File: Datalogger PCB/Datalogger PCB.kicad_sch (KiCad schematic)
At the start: 50 parts, among them J1 Conn_01x02_Pin, M1 Motor_Servo, M2 Motor_Servo, M3 Motor_Servo, M4 Motor_Servo, U1 Teensy4.1, U2 BNO055, U3 LPS25HB, U4 AMS1117-5.0, U5 NRF24L01_Breakout, U6 VN5E160STR-E, U7 VN5E160STR-E, U8 VN5E160STR-E, U9 VN5E160STR-E

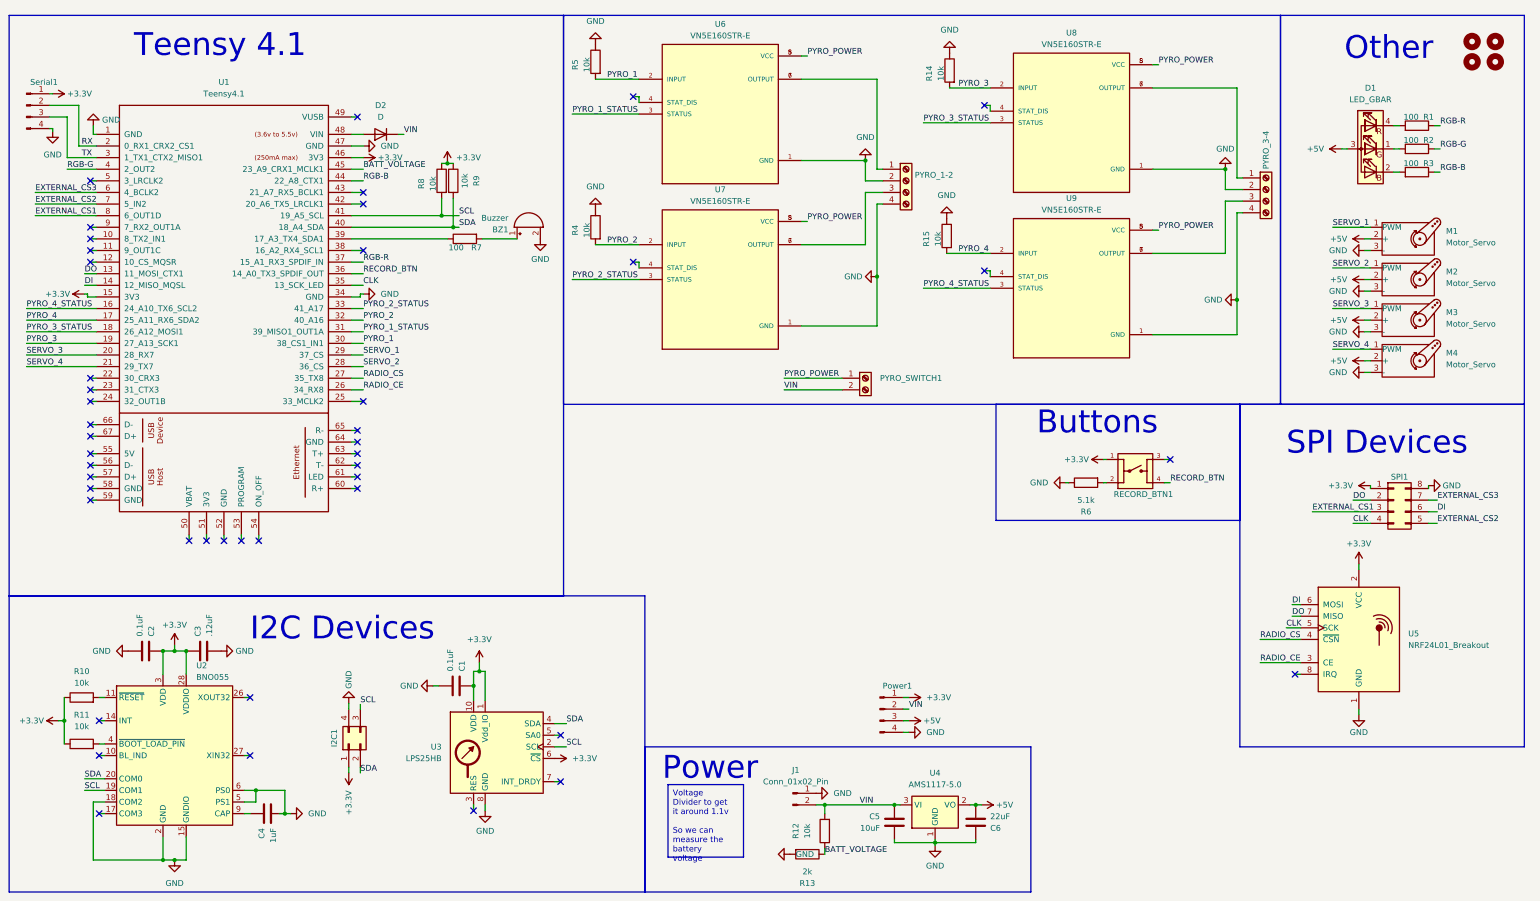
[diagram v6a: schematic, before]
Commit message: Modified the 5v power rail a little
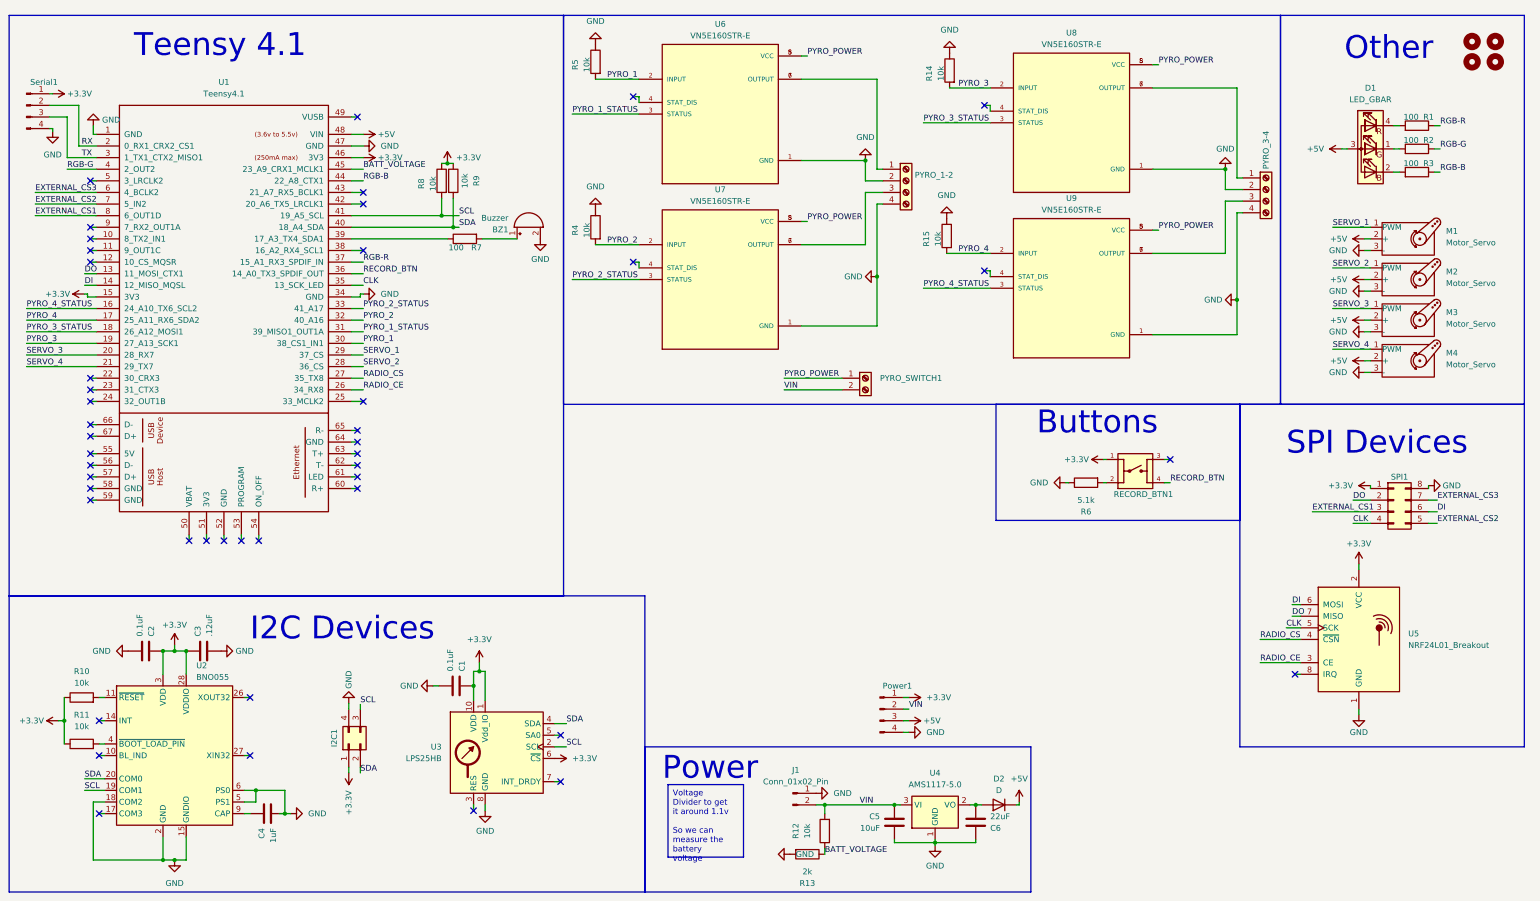
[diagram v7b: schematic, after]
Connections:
- net +5V: now also D2.1 (K), U1.48 (VIN); no longer C6.2, U4.2 (VO)
- net VIN: no longer D2.1 (K)
- net at D2.2 (A): now also C6.2, U4.2 (VO); no longer U1.48 (VIN)
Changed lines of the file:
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@@
   (junction (at 278.13 45.72) (diameter 0) (color 0 0 0 0)
   )
+  (junction (at 223.52 184.785) (diameter 0) (color 0 0 0 0)
+  )
   (junction (at 214.63 193.04) (diameter 0) (color 0 0 0 0)
   )
@@
   (junction (at 66.04 181.61) (diameter 0) (color 0 0 0 0)
   )
-  (junction (at 223.52 184.785) (diameter 0) (color 0 0 0 0)
-  )
   (junction (at 190.5 184.785) (diameter 0) (color 0 0 0 0)
   )
@@
     (stroke (width 0) (type default))
   )
+  (wire (pts (xy 233.045 184.15) (xy 233.045 184.785))
+    (stroke (width 0) (type default))
+  )
   (wire (pts (xy 301.625 76.2) (xy 309.88 76.2))
     (stroke (width 0) (type default))
@@
     (stroke (width 0) (type default))
   )
-  (wire (pts (xy 89.535 38.1) (xy 86.995 38.1))
+  (wire (pts (xy 233.045 184.785) (xy 232.41 184.785))
     (stroke (width 0) (type default))
   )
@@
     (stroke (width 0) (type default))
   )
+  (wire (pts (xy 224.79 184.785) (xy 223.52 184.785))
+    (stroke (width 0) (type default))
+  )
   (wire (pts (xy 307.34 165.1) (xy 307.34 163.83))
     (stroke (width 0) (type default))
@@
     (stroke (width 0) (type default))
   )
-  (wire (pts (xy 224.79 184.785) (xy 223.52 184.785))
-    (stroke (width 0) (type default))
-  )
   (wire (pts (xy 88.9 176.53) (xy 88.9 177.8))
     (stroke (width 0) (type default))
@@
     (stroke (width 0) (type default))
   )
+  (wire (pts (xy 89.535 38.1) (xy 86.995 38.1))
+    (stroke (width 0) (type default))
+  )
   (wire (pts (xy 21.59 36.83) (xy 20.955 36.83))
     (stroke (width 0) (type default))
@@
     (stroke (width 0) (type default))
   )
-  (wire (pts (xy 98.425 38.1) (xy 97.155 38.1))
-    (stroke (width 0) (type default))
-  )
   (wire (pts (xy 148.59 66.04) (xy 149.86 66.04))
     (stroke (width 0) (type default))
@@
     (effects (font (size 1.27 1.27)) (justify left bottom))
   )
-  (label "VIN" (at 98.425 38.1 0) (fields_autoplaced)
-    (effects (font (size 1.27 1.27)) (justify left bottom))
-  )
   (label "RADIO_CE" (at 89.535 93.98 0) (fields_autoplaced)
     (effects (font (size 1.27 1.27)) (justify left bottom))
@@
     )
   )
-  (symbol (lib_id "power:+5V") (at 224.79 184.785 270) (unit 1)
+  (symbol (lib_id "power:+5V") (at 233.045 184.15 0) (unit 1)
     (in_bom yes) (on_board yes) (dnp no) (fields_autoplaced)
-    (property "Reference" "#PWR039" (at 220.98 184.785 0)
+    (property "Reference" "#PWR039" (at 233.045 187.96 0)
       (effects (font (size 1.27 1.27)) hide)
     )
-    (property "Value" "+5V" (at 227.965 184.785 90)
-      (effects (font (size 1.27 1.27)) (justify left))
+    (property "Value" "+5V" (at 233.045 179.07 0)
+      (effects (font (size 1.27 1.27)))
     )
-    (property "Footprint" "" (at 224.79 184.785 0)
+    (property "Footprint" "" (at 233.045 184.15 0)
       (effects (font (size 1.27 1.27)) hide)
     )
-    (property "Datasheet" "" (at 224.79 184.785 0)
+    (property "Datasheet" "" (at 233.045 184.15 0)
       (effects (font (size 1.27 1.27)) hide)
     )
@@
     )
   )
+  (symbol (lib_id "Device:D") (at 228.6 184.785 180) (unit 1)
+    (in_bom yes) (on_board yes) (dnp no) (fields_autoplaced)
+    (property "Reference" "D2" (at 228.6 179.07 0)
+      (effects (font (size 1.27 1.27)))
+    )
+    (property "Value" "D" (at 228.6 181.61 0)
+      (effects (font (size 1.27 1.27)))
+    )
+    (property "Footprint" "Diode_SMD:D_0603_1608Metric_Pad1.05x0.95mm_HandSolder" (at 228.6 184.785 0)
+      (effects (font (size 1.27 1.27)) hide)
+    )
+    (property "Datasheet" "~" (at 228.6 184.785 0)
+      (effects (font (size 1.27 1.27)) hide)
+    )
+    (property "Sim.Device" "D" (at 228.6 184.785 0)
+      (effects (font (size 1.27 1.27)) hide)
+    )
+    (property "Sim.Pins" "1=K 2=A" (at 228.6 184.785 0)
+      (effects (font (size 1.27 1.27)) hide)
+    )
+    (pin "1")
+    (pin "2")
+    (instances
+      (project "Datalogger PCB"
+        (path "/a3bc5533-d6ac-45b5-a7d9-fc1b12646794"
+          (reference "D2") (unit 1)
+        )
+      )
+    )
+  )
   (symbol (lib_id "power:+3.3V") (at 251.46 109.22 90) (unit 1)
     (in_bom yes) (on_board yes) (dnp no) (fields_autoplaced)
@@
     )
   )
+  (symbol (lib_id "power:+5V") (at 89.535 38.1 270) (unit 1)
+    (in_bom yes) (on_board yes) (dnp no) (fields_autoplaced)
+    (property "Reference" "#PWR027" (at 85.725 38.1 0)
+      (effects (font (size 1.27 1.27)) hide)
+    )
+    (property "Value" "+5V" (at 92.71 38.1 90)
+      (effects (font (size 1.27 1.27)) (justify left))
+    )
+    (property "Footprint" "" (at 89.535 38.1 0)
+      (effects (font (size 1.27 1.27)) hide)
+    )
+    (property "Datasheet" "" (at 89.535 38.1 0)
+      (effects (font (size 1.27 1.27)) hide)
+    )
+    (pin "1")
+    (instances
+      (project "Datalogger PCB"
+        (path "/a3bc5533-d6ac-45b5-a7d9-fc1b12646794"
+          (reference "#PWR027") (unit 1)
+        )
+      )
+    )
+  )
   (symbol (lib_id "power:GND") (at 308.61 90.17 270) (mirror x) (unit 1)
     (in_bom yes) (on_board yes) (dnp no) (fields_autoplaced)
@@
         )
       )
-    )
-  )
-  (symbol (lib_id "Device:D") (at 93.345 38.1 180) (unit 1)
-    (in_bom yes) (on_board yes) (dnp no) (fields_autoplaced)
-    (property "Reference" "D2" (at 93.345 31.75 0)
-      (effects (font (size 1.27 1.27)))
-    )
-    (property "Value" "D" (at 93.345 34.29 0)
-      (effects (font (size 1.27 1.27)))
-    )
-    (property "Footprint" "Diode_SMD:D_0603_1608Metric_Pad1.05x0.95mm_HandSolder" (at 93.345 38.1 0)
-      (effects (font (size 1.27 1.27)) hide)
-    )
-    (property "Datasheet" "~" (at 93.345 38.1 0)
-      (effects (font (size 1.27 1.27)) hide)
-    )
-    (property "Sim.Device" "D" (at 93.345 38.1 0)
-      (effects (font (size 1.27 1.27)) hide)
-    )
-    (property "Sim.Pins" "1=K 2=A" (at 93.345 38.1 0)
-      (effects (font (size 1.27 1.27)) hide)
-    )
-    (pin "2")
-    (pin "1")
-    (instances
-      (project "Datalogger PCB"
-        (path "/a3bc5533-d6ac-45b5-a7d9-fc1b12646794"
-          (reference "D2") (unit 1)
-        )
-      )

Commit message: Made connectors bigger and removed unused radio connector
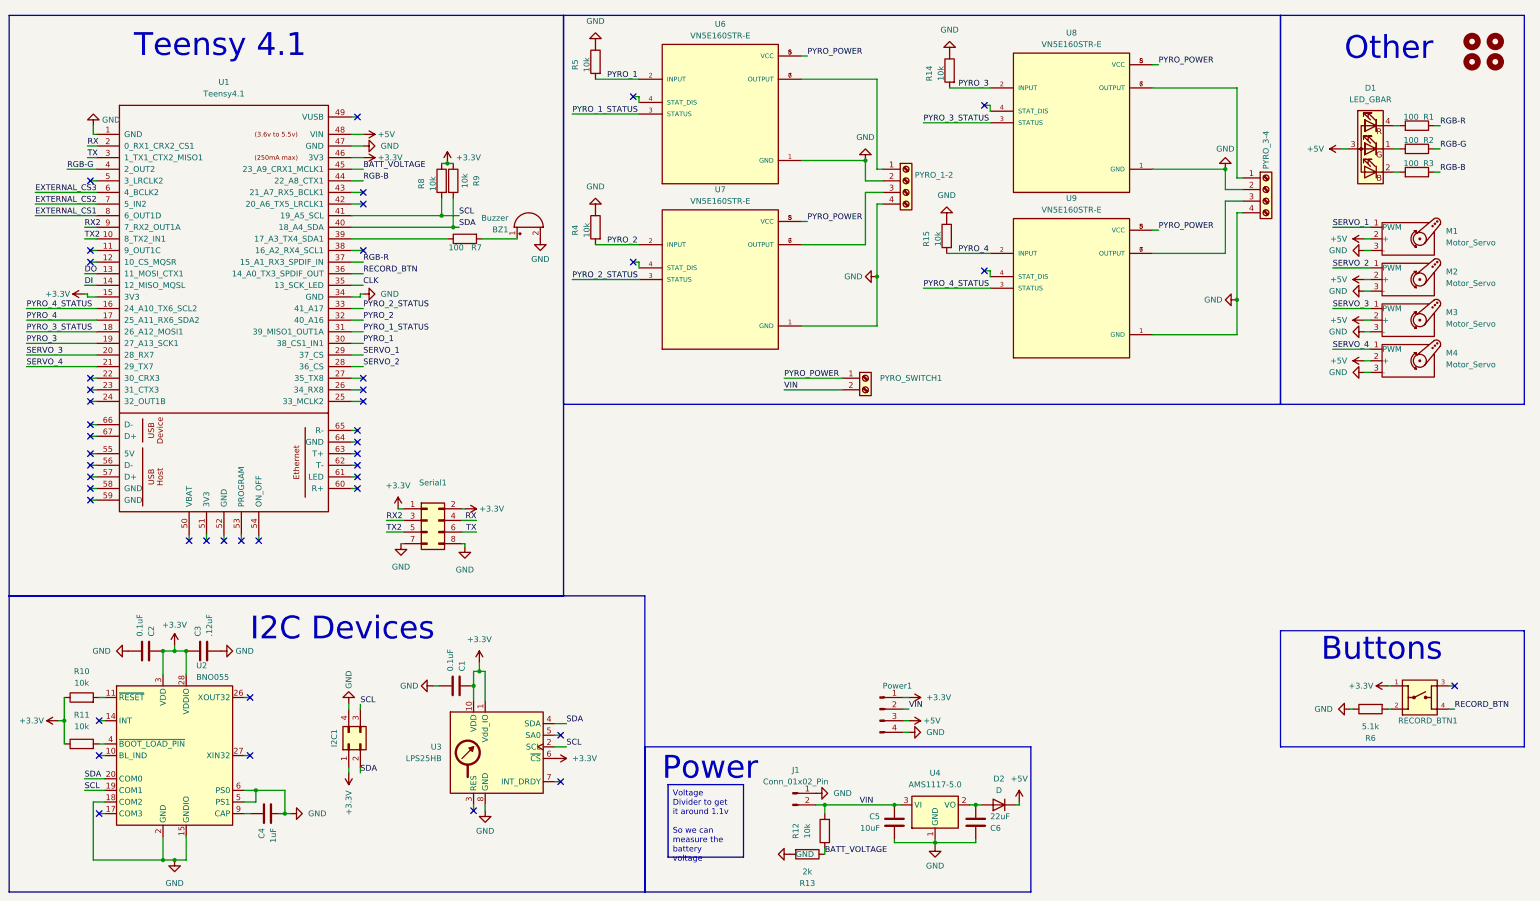
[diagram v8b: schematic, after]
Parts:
- removed SPI1: Conn_02x04_Counter_Clockwise, Connector_PinHeader_1.27mm:PinHeader_2x04_P1.27mm_Vertical, symbol Connector_Generic:Conn_02x04_Counter_Clockwise
- removed Serial1: Conn_01x04_Pin, Connector_PinHeader_1.27mm:PinHeader_1x04_P1.27mm_Vertical, symbol Connector:Conn_01x04_Pin
- removed U5: NRF24L01_Breakout, RF_Module:nRF24L01_Breakout, symbol RF:NRF24L01_Breakout
- added Serial1: Conn_02x04_Odd_Even, Connector_PinSocket_2.54mm:PinSocket_2x04_P2.54mm_Vertical, symbol Connector_Generic:Conn_02x04_Odd_Even
- H1, H2, H3, H4: footprint MountingHole:MountingHole_2.2mm_M2 -> MountingHole:MountingHole_3.2mm_M3
- I2C1: footprint Connector_PinHeader_1.27mm:PinHeader_2x02_P1.27mm_Vertical -> Connector_PinSocket_2.54mm:PinSocket_2x02_P2.54mm_Vertical
- Power1: footprint Connector_PinHeader_1.27mm:PinHeader_1x04_P1.27mm_Vertical -> Connector_PinSocket_2.54mm:PinSocket_1x04_P2.54mm_Vertical
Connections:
- net +3.3V: now also Serial1.1 (Pin_1), Serial1.2 (Pin_2)
- net GND: now also Serial1.7 (Pin_7), Serial1.8 (Pin_8)
- net RX: now also Serial1.4 (Pin_4)
- net TX: now also Serial1.6 (Pin_6)
- net TX2: now reaches U1.10 (8_TX2_IN1)
- net TX2: now also Serial1.5 (Pin_5)
- net RX2: now reaches U1.9 (7_RX2_OUT1A)
- net RX2: now also Serial1.3 (Pin_3)
- net RADIO_CE: no longer names the net of U1.26 (34_RX8)
- net RADIO_CS: no longer names the net of U1.27 (35_TX8)
- no-connect marks 45 -> 44
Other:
- note removed: "SPI Devices"
- moved on the sheet: R6, RECORD_BTN1
